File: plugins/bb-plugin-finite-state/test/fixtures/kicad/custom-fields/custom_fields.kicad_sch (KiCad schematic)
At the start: 2 parts, among them J1 Conn_01x02

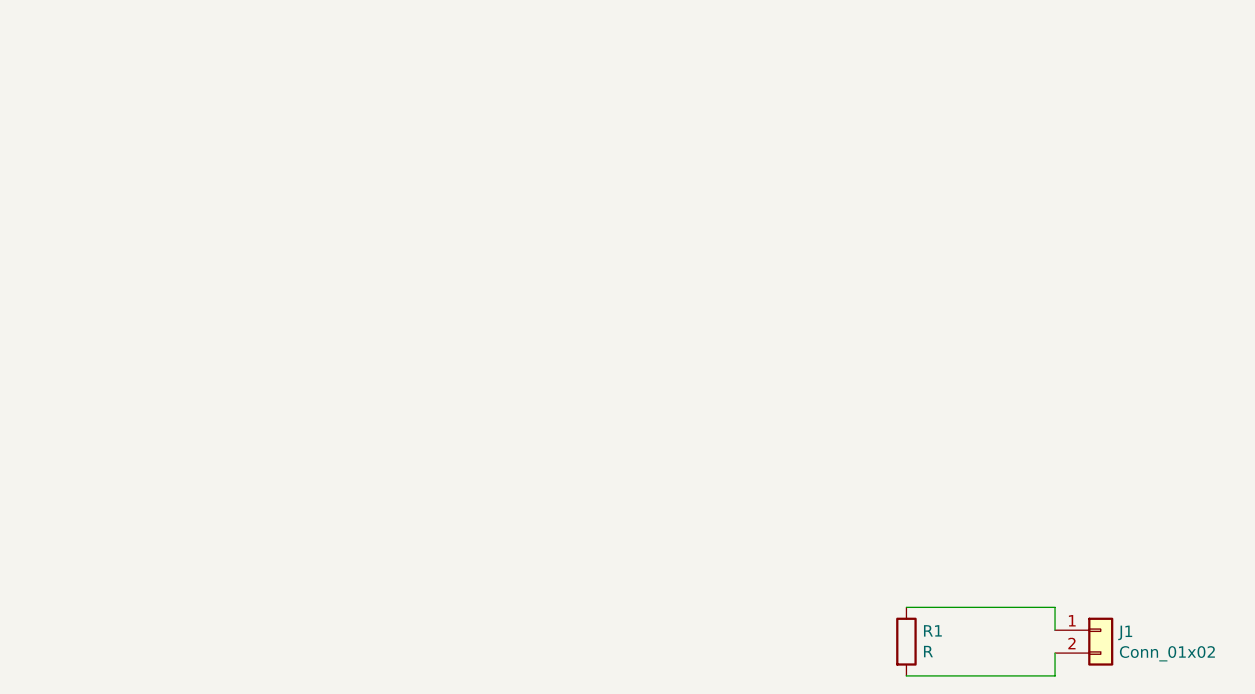
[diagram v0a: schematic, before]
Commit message: fs plugin: replace GPL KiCad fixture
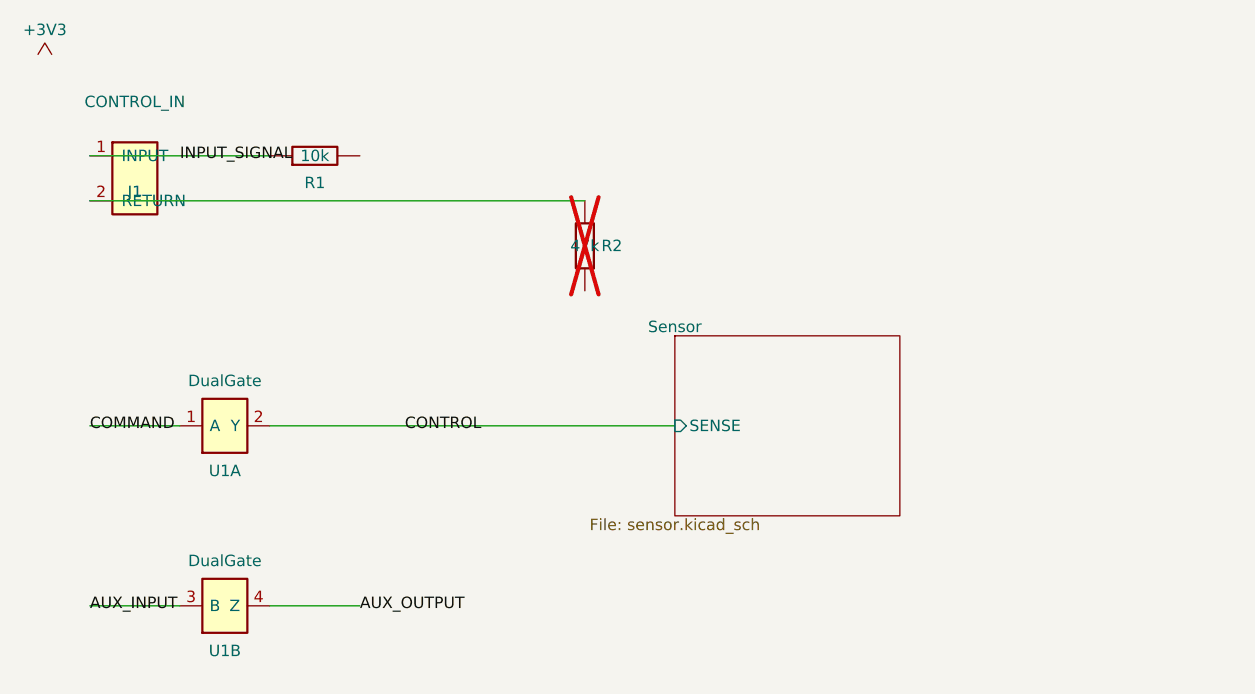
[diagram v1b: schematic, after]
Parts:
- removed J1: Conn_01x02, Connector_JST:JST_XH_B2B-XH-A_1x02_P2.50mm_Vertical, symbol Connector_Generic:Conn_01x02
- removed R1: R, Resistor_SMD:R_1206_3216Metric, symbol Device:R
- added J1: CONTROL_IN, Fixture:Header_1x02, symbol Fixture:Conn_01x02
- added R1: 10k, Fixture:R_0603, symbol Fixture:R
- added R2: 47k, Fixture:R_0603, symbol Fixture:R
- added U1: DualGate, Fixture:TSSOP-8, symbol Fixture:DualGate
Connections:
- new net: J1.2 (RETURN), R2.2
- new net AUX_INPUT: U1.3 (B)
- new net AUX_OUTPUT: U1.4 (Z)
- new net COMMAND: U1.1 (A)
- new net CONTROL: U1.2 (Y)
- new net INPUT_SIGNAL: J1.1 (INPUT), R1.1
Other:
- added sheet Sensor (sensor.kicad_sch)
